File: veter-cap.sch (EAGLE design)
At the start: 36 parts, among them IC1 7805TV

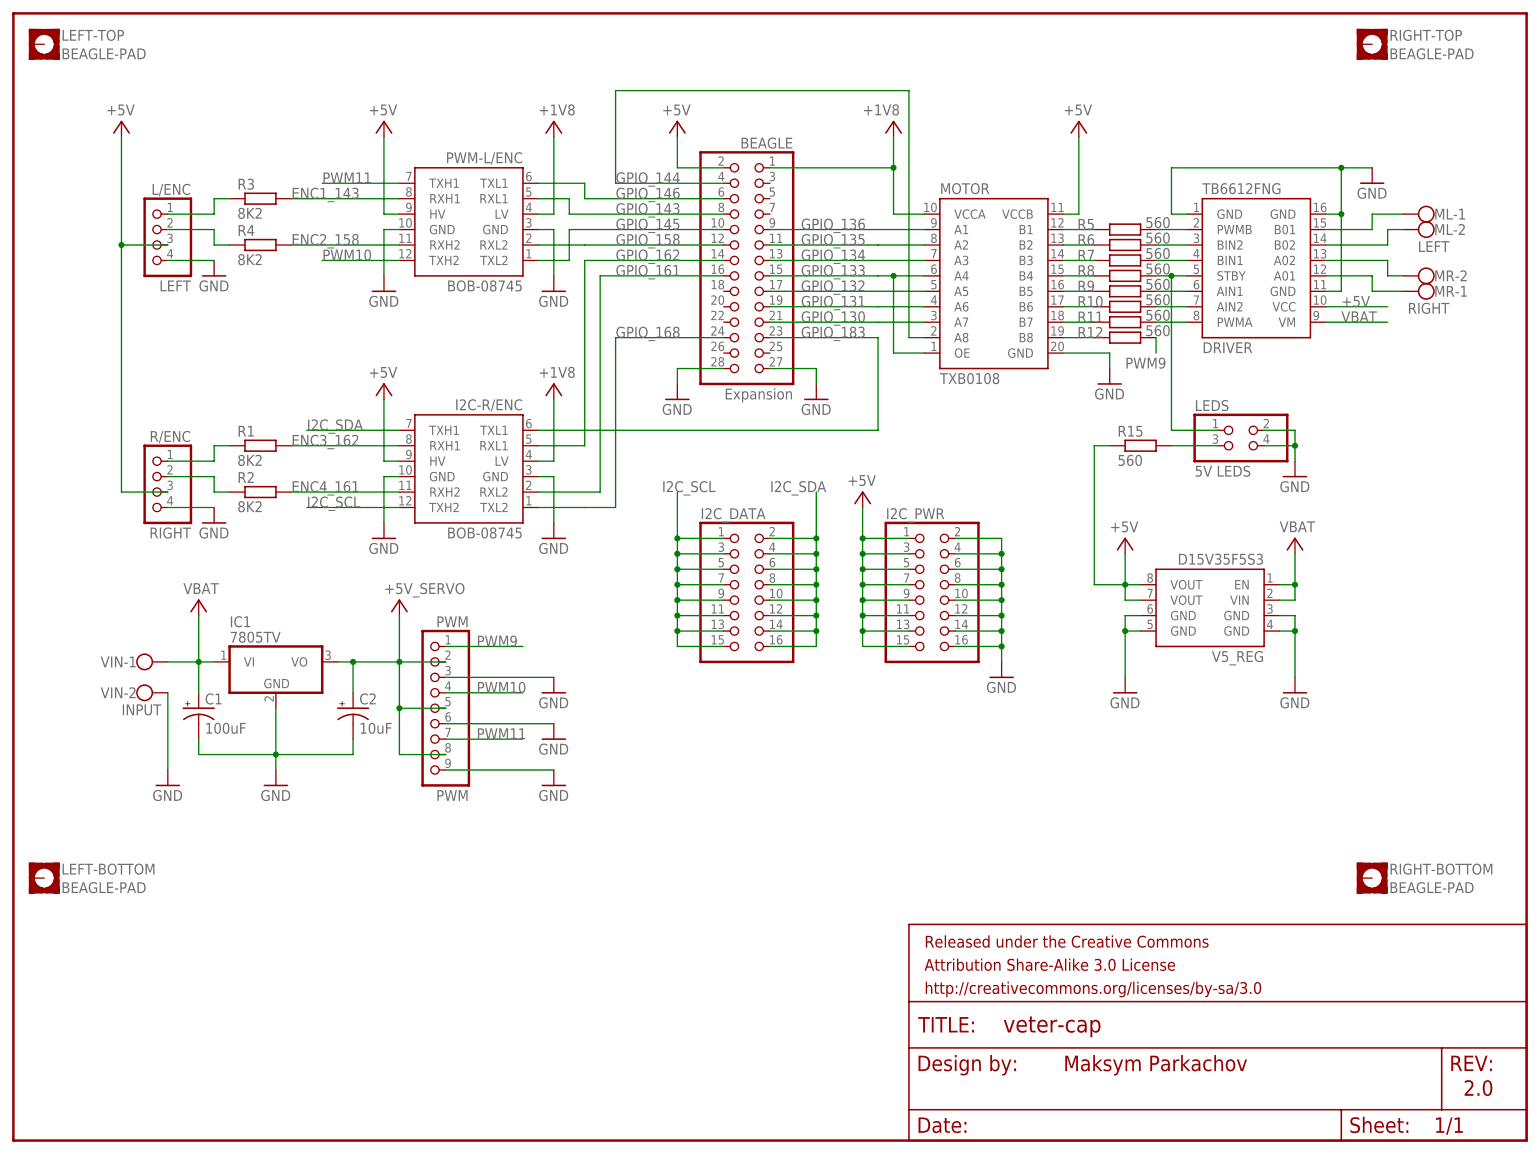
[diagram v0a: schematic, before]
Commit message: version 3.0 of the cap, fixed connector
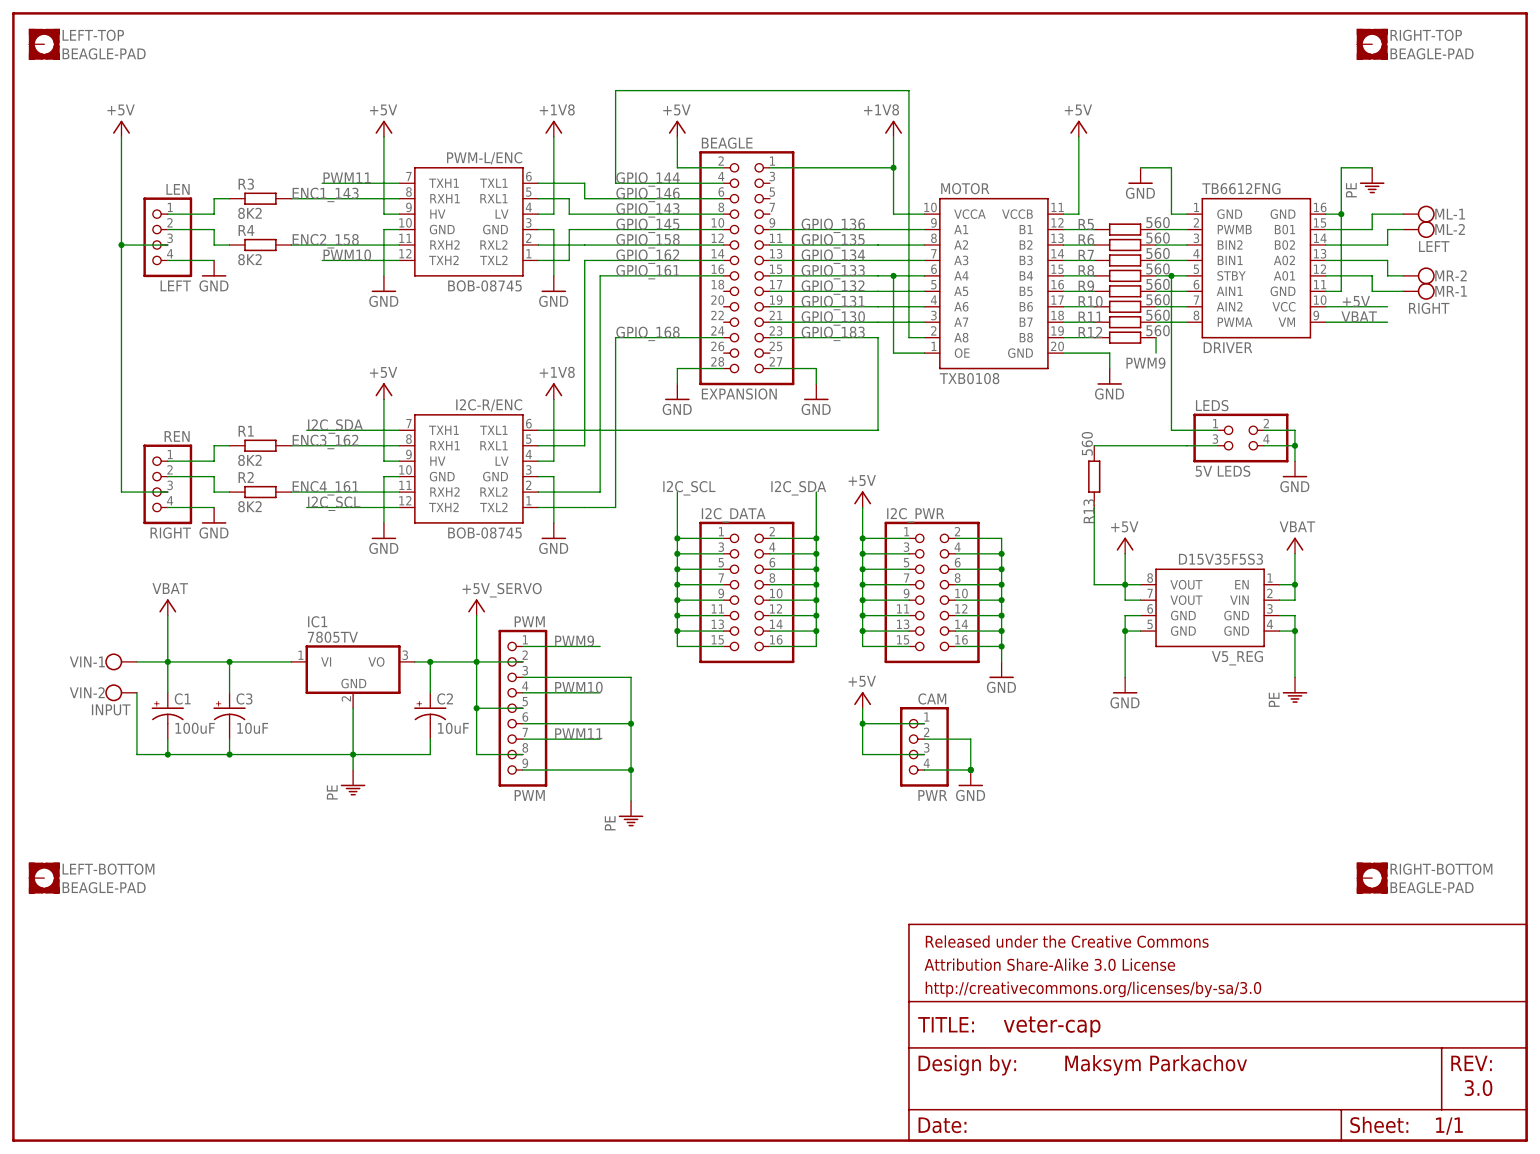
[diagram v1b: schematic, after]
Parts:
- removed R15: 560, resistor:R-EU_0207/5V
- added C3: 10uF, SparkFun-Passives:CAP_POLPTH2
- added CAM: PWR, pinhead:PINHD-1X4/90
- added R13: 560, resistor:R-EU_0207/10
- BEAGLE: value Expansion -> EXPANSION; device pinhead:PINHD-2X14 -> veter:BEAGLE_EXPANSION
- renumbered L/ENC to LEN, R/ENC to REN
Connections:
- removed net GND: BEAGLE.27, BEAGLE.28, C1.-, C2.-, DRIVER.GND@1, DRIVER.GND@2, DRIVER.GND@3, I2C-R/ENC.GND@1, I2C-R/ENC.GND@2, I2C_PWR.10, I2C_PWR.12, I2C_PWR.14, I2C_PWR.16, I2C_PWR.2, I2C_PWR.4, I2C_PWR.6, I2C_PWR.8, IC1.GND, LEDS.2, LEDS.4, LEN.4, MOTOR.GND, PWM-L/ENC.GND@1, PWM-L/ENC.GND@2, PWM.3, PWM.6, PWM.9, REN.4, V5_REG.GND@1, V5_REG.GND@2, V5_REG.GND@3, V5_REG.GND@4, VIN-2.KL
- new net OE: BEAGLE.27, BEAGLE.28, CAM.2, CAM.4, DRIVER.GND@1, I2C-R/ENC.GND@1, I2C-R/ENC.GND@2, I2C_PWR.10, I2C_PWR.12, I2C_PWR.14, I2C_PWR.16, I2C_PWR.2, I2C_PWR.4, I2C_PWR.6, I2C_PWR.8, LEDS.2, LEDS.4, LEN.4, MOTOR.GND, PWM-L/ENC.GND@1, PWM-L/ENC.GND@2, REN.4, V5_REG.GND@3, V5_REG.GND@4
- new net PE: C1.-, C2.-, C3.-, DRIVER.GND@2, DRIVER.GND@3, IC1.GND, PWM.3, PWM.6, PWM.9, V5_REG.GND@1, V5_REG.GND@2, VIN-2.KL
- net +5V: now also CAM.1, CAM.3, R13.1; no longer R15.1
- net N$24: now also R13.2; no longer R15.2
- net VBAT: now also C3.+
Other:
- note added: "3.0"
- note removed: "2.0"
- moved on the sheet: C1, C2, IC1, PWM, VIN-1, VIN-2
